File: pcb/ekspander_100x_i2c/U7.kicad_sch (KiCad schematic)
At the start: 6 parts, among them J18 DG127A-5.08-06P-14-00AH, J19 DG127A-5.08-06P-14-00AH, J20 DG127A-5.08-06P-14-00AH, J21 DG127A-5.08-06P-14-00AH, U7 MCP23017_SP, U8 MCP23017_SP

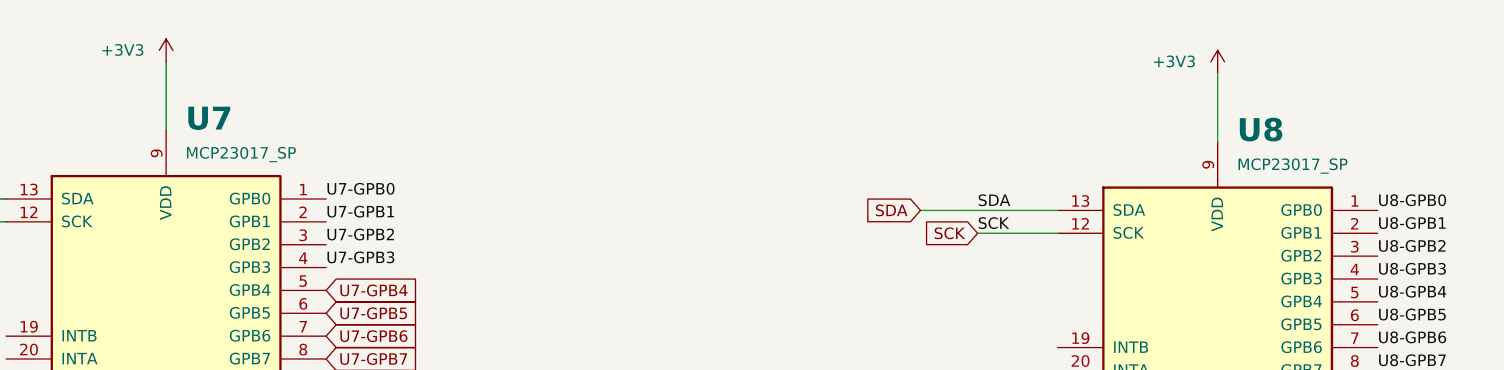
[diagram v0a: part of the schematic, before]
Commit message: Ekspander U2 - U3 - U4 update
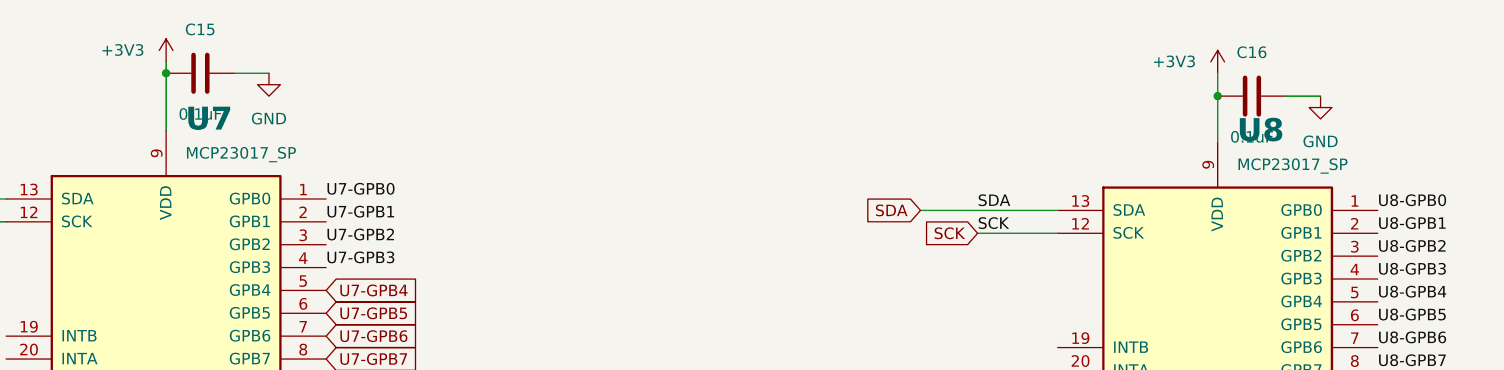
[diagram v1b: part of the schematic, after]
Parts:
- added C15, C16: 0.1uF, Capacitor_SMD:C_0805_2012Metric_Pad1.18x1.45mm_HandSolder, symbol Device:C
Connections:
- net +3V3: now also C15.1, C16.1
- net GND: now also C15.2, C16.2

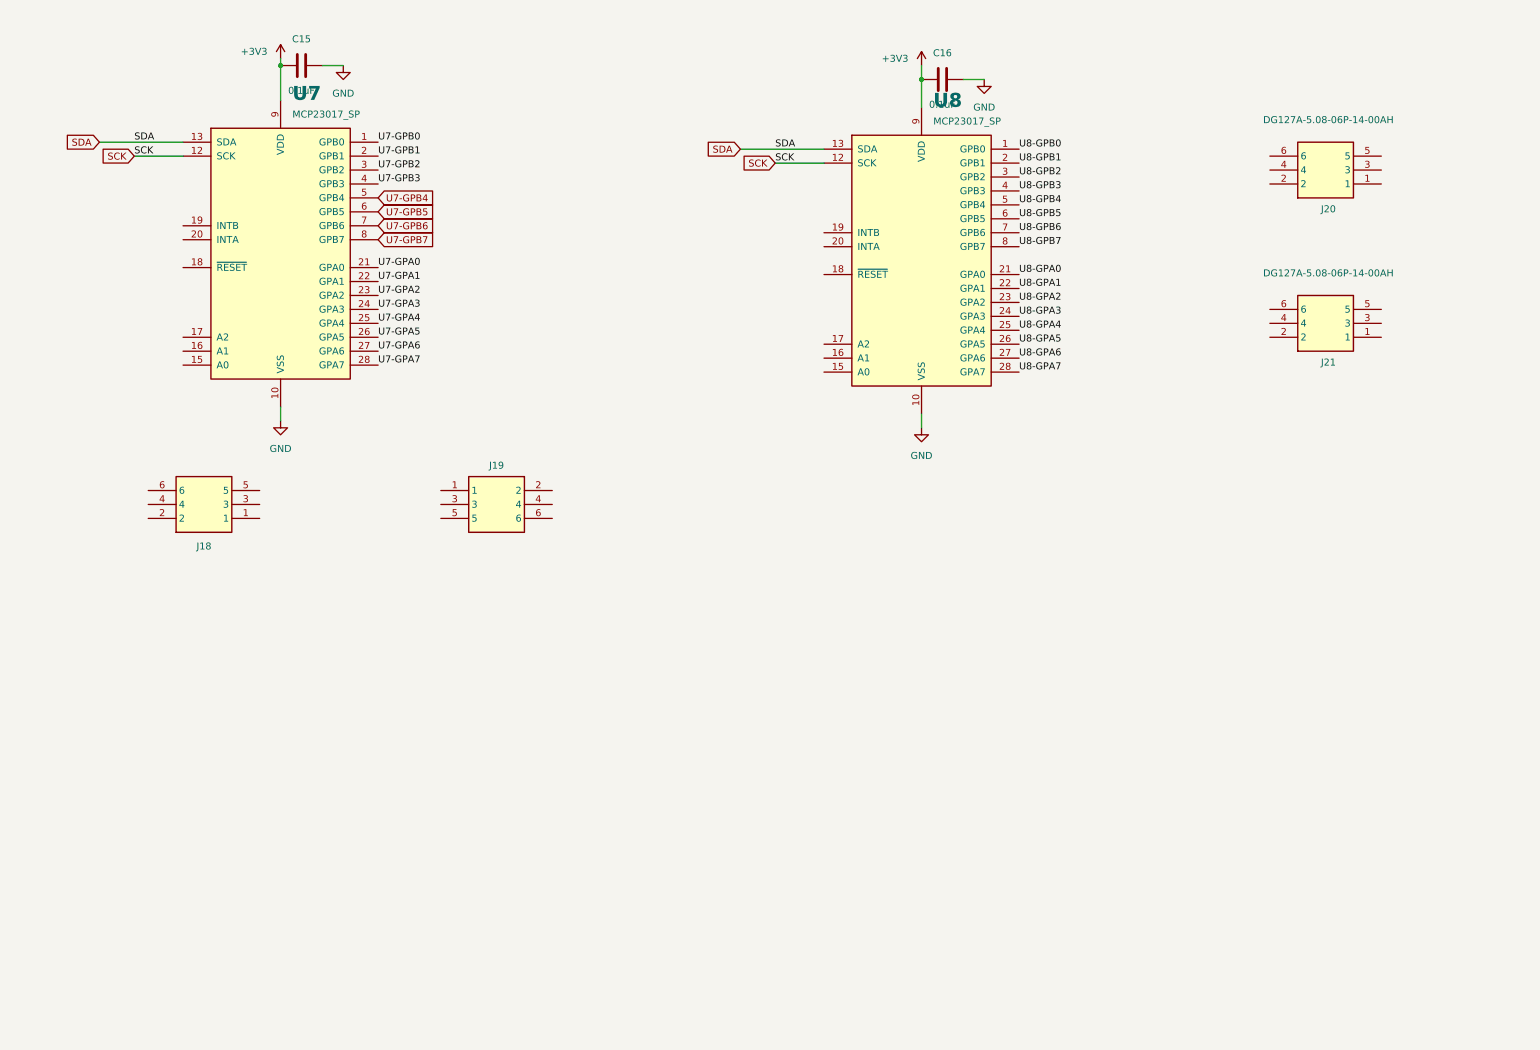
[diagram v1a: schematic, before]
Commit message: Ekspander 24V update
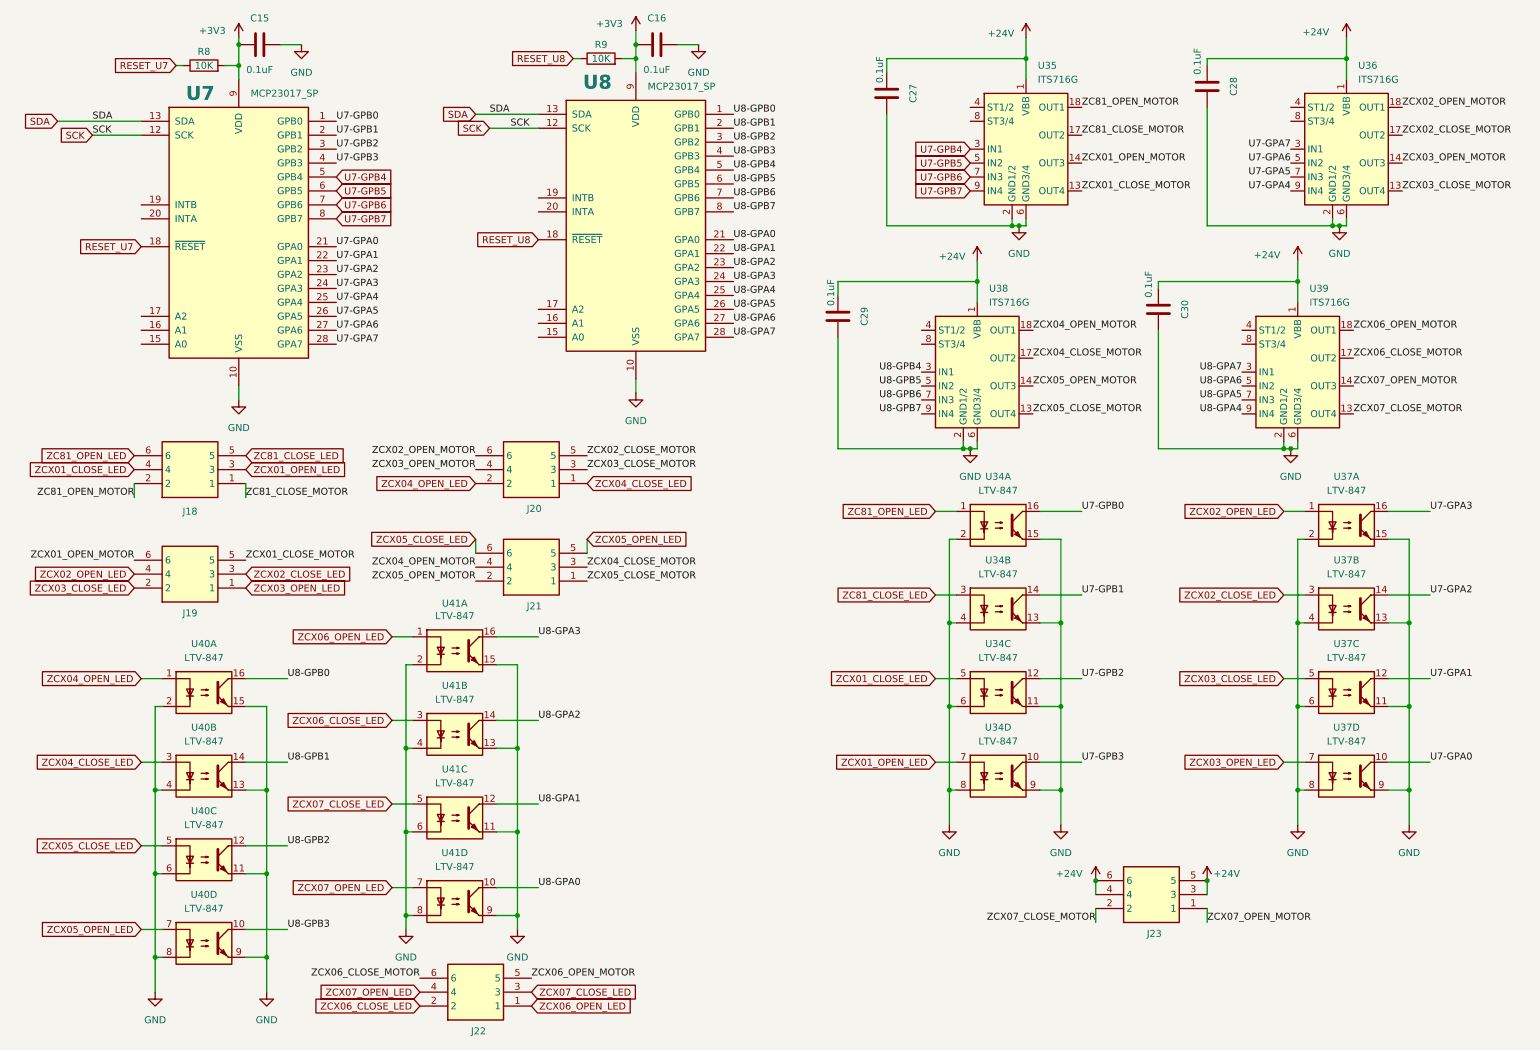
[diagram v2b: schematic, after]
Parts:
- added C27, C28, C29, C30: 0.1uF, Capacitor_SMD:C_0805_2012Metric_Pad1.18x1.45mm_HandSolder, symbol Device:C
- added J22, J23: DG127A-5.08-06P-14-00AH, DG127A50806P1400AH, symbol 1_tme:DG127A-5.08-06P-14-00AH
- added R8, R9: 10K, PCM_Resistor_SMD_AKL:R_0805_2012Metric_Pad1.20x1.40mm_HandSolder, symbol Device:R
- added U34, U37, U40, U41: LTV-847, Package_DIP:DIP-16_W7.62mm, symbol Isolator:LTV-847
- added U35, U36, U38, U39: ITS716G, Package_SO:SOIC-20W_7.5x12.8mm_P1.27mm, symbol Driver_FET:ITS716G
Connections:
- net +3V3: now also R8.2, R9.2
- net GND: now also C27.2, C28.2, C29.2, C30.2, U34.11, U34.13, U34.15, U34.2, U34.4, U34.6, U34.8, U34.9, U35.2 (GND1/2), U35.6 (GND3/4), U36.2 (GND1/2), U36.6 (GND3/4), U37.11, U37.13, U37.15, U37.2, U37.4, U37.6, U37.8, U37.9, U38.2 (GND1/2), U38.6 (GND3/4), U39.2 (GND1/2), U39.6 (GND3/4), U40.11, U40.13, U40.15, U40.2, U40.4, U40.6, U40.8, U40.9, U41.11, U41.13, U41.15, U41.2, U41.4, U41.6, U41.8, U41.9
- net U7-GPA0: now also U37.10
- net U7-GPA1: now also U37.12
- net U7-GPA2: now also U37.14
- net U7-GPA3: now also U37.16
- net U7-GPA4: now also U36.9 (IN4)
- net U7-GPA5: now also U36.7 (IN3)
- net U7-GPA6: now also U36.5 (IN2)
- net U7-GPA7: now also U36.3 (IN1)
- net U7-GPB0: now also U34.16
- net U7-GPB1: now also U34.14
- net U7-GPB2: now also U34.12
- net U7-GPB3: now also U34.10
- net U7-GPB4: now also U35.3 (IN1)
- net U7-GPB5: now also U35.5 (IN2)
- net U7-GPB6: now also U35.7 (IN3)
- net U7-GPB7: now also U35.9 (IN4)
- net U8-GPA0: now also U41.10
- net U8-GPA1: now also U41.12
- net U8-GPA2: now also U41.14
- net U8-GPA3: now also U41.16
- net U8-GPA4: now also U39.9 (IN4)
- net U8-GPA5: now also U39.7 (IN3)
- net U8-GPA6: now also U39.5 (IN2)
- net U8-GPA7: now also U39.3 (IN1)
- net U8-GPB0: now also U40.16
- net U8-GPB1: now also U40.14
- net U8-GPB2: now also U40.12
- net U8-GPB3: now also U40.10
- net U8-GPB4: now also U38.3 (IN1)
- net U8-GPB5: now also U38.5 (IN2)
- net U8-GPB6: now also U38.7 (IN3)
- net U8-GPB7: now also U38.9 (IN4)
- net RESET_U8: now reaches U8.18 (~{RESET})
- net RESET_U8: now also R9.1
- net ZCX04_CLOSE_LED: now reaches J20.1
- net ZCX04_CLOSE_LED: now also U40.3
- net ZCX04_OPEN_LED: now reaches J20.2
- net ZCX04_OPEN_LED: now also U40.1
- net ZCX03_CLOSE_MOTOR: now reaches J20.3
- net ZCX03_CLOSE_MOTOR: now also U36.13 (OUT4)
- net ZCX03_OPEN_MOTOR: now reaches J20.4
- net ZCX03_OPEN_MOTOR: now also U36.14 (OUT3)
- net ZCX02_CLOSE_MOTOR: now reaches J20.5
- net ZCX02_CLOSE_MOTOR: now also U36.17 (OUT2)
- net ZCX02_OPEN_MOTOR: now reaches J20.6
- net ZCX02_OPEN_MOTOR: now also U36.18 (OUT1)
- net RESET_U7: now reaches U7.18 (~{RESET})
- net RESET_U7: now also R8.1
- net ZCX03_OPEN_LED: now reaches J19.1
- net ZCX03_OPEN_LED: now also U37.7
- net ZCX03_CLOSE_LED: now reaches J19.2
- net ZCX03_CLOSE_LED: now also U37.5
- net ZCX02_CLOSE_LED: now reaches J19.3
- net ZCX02_CLOSE_LED: now also U37.3
- net ZCX02_OPEN_LED: now reaches J19.4
- net ZCX02_OPEN_LED: now also U37.1
- net ZCX01_CLOSE_MOTOR: now reaches J19.5
- net ZCX01_CLOSE_MOTOR: now also U35.13 (OUT4)
- net ZCX01_OPEN_MOTOR: now reaches J19.6
- net ZCX01_OPEN_MOTOR: now also U35.14 (OUT3)
- net ZC81_CLOSE_MOTOR: now reaches J18.1
- net ZC81_CLOSE_MOTOR: now also U35.17 (OUT2)
- net ZC81_OPEN_MOTOR: now reaches J18.2
- net ZC81_OPEN_MOTOR: now also U35.18 (OUT1)
- net ZCX01_OPEN_LED: now reaches J18.3
- net ZCX01_OPEN_LED: now also U34.7
- net ZCX01_CLOSE_LED: now reaches J18.4
- net ZCX01_CLOSE_LED: now also U34.5
- net ZC81_CLOSE_LED: now reaches J18.5
- net ZC81_CLOSE_LED: now also U34.3
- net ZC81_OPEN_LED: now reaches J18.6
- net ZC81_OPEN_LED: now also U34.1
- net ZCX05_CLOSE_MOTOR: now reaches J21.1
- net ZCX05_CLOSE_MOTOR: now also U38.13 (OUT4)
- net ZCX05_OPEN_MOTOR: now reaches J21.2
- net ZCX05_OPEN_MOTOR: now also U38.14 (OUT3)
- net ZCX04_CLOSE_MOTOR: now reaches J21.3
- net ZCX04_CLOSE_MOTOR: now also U38.17 (OUT2)
- net ZCX04_OPEN_MOTOR: now reaches J21.4
- net ZCX04_OPEN_MOTOR: now also U38.18 (OUT1)
- net ZCX05_OPEN_LED: now reaches J21.5
- net ZCX05_OPEN_LED: now also U40.7
- net ZCX05_CLOSE_LED: now reaches J21.6
- net ZCX05_CLOSE_LED: now also U40.5
- new net +24V: C27.1, C28.1, C29.1, C30.1, J23.3, J23.4, J23.5, J23.6, U35.1 (VBB), U35.10 (VBB), U35.11 (VBB), U35.12 (VBB), U35.15 (VBB), U35.16 (VBB), U35.19 (VBB), U35.20 (VBB), U36.1 (VBB), U36.10 (VBB), U36.11 (VBB), U36.12 (VBB), U36.15 (VBB), U36.16 (VBB), U36.19 (VBB), U36.20 (VBB), U38.1 (VBB), U38.10 (VBB), U38.11 (VBB), U38.12 (VBB), U38.15 (VBB), U38.16 (VBB), U38.19 (VBB), U38.20 (VBB), U39.1 (VBB), U39.10 (VBB), U39.11 (VBB), U39.12 (VBB), U39.15 (VBB), U39.16 (VBB), U39.19 (VBB), U39.20 (VBB)
- new net ZCX06_CLOSE_LED: J22.2, U41.3
- new net ZCX06_CLOSE_MOTOR: J22.6, U39.17 (OUT2)
- new net ZCX06_OPEN_LED: J22.1, U41.1
- new net ZCX06_OPEN_MOTOR: J22.5, U39.18 (OUT1)
- new net ZCX07_CLOSE_LED: J22.3, U41.5
- new net ZCX07_CLOSE_MOTOR: J23.2, U39.13 (OUT4)
- new net ZCX07_OPEN_LED: J22.4, U41.7
- new net ZCX07_OPEN_MOTOR: J23.1, U39.14 (OUT3)
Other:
- moved on the sheet: C15, C16, J18, J19, J20, J21, U7, U8
